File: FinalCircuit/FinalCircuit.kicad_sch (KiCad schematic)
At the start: 54 parts, among them J1 Conn_02x20_Odd_Even, J2 Conn_02x05_Odd_Even, J3 Conn_01x06, U1 LM6172, U10 CD4066BE, U11 CD4066BE, U2 OPA2277, U3 MCP3008, U4 MCP4921, U5 CD4066BE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

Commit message: Almost all connections done. Digital traces seem too long at the moment.
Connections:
- net ADC_CSbar: now also J1.10 (Pin_10); no longer J1.34 (Pin_34)
- net CLK: now also J1.18 (Pin_18); no longer J1.39 (Pin_39)
- net Control1: now also J1.15 (Pin_15); no longer J1.9 (Pin_9)
- net Control10A: now also J1.27 (Pin_27); no longer J1.19 (Pin_19)
- net Control10B: now also J1.21 (Pin_21); no longer J1.15 (Pin_15)
- net Control2: now also J1.39 (Pin_39); no longer J1.6 (Pin_6)
- net Control3: now also J1.37 (Pin_37); no longer J1.8 (Pin_8)
- net Control4: now also J1.17 (Pin_17); no longer J1.10 (Pin_10)
- net Control5: now also J1.7 (Pin_7); no longer J1.14 (Pin_14)
- net Control6: now also J1.8 (Pin_8); no longer J1.16 (Pin_16)
- net Control7: now also J1.9 (Pin_9); no longer J1.5 (Pin_5)
- net Control8: now also J1.6 (Pin_6); no longer J1.7 (Pin_7)
- net Control9A: now also J1.19 (Pin_19); no longer J1.13 (Pin_13)
- net Control9B: now also J1.35 (Pin_35); no longer J1.17 (Pin_17)
- net ControlMain_ReadWrite: now also J1.4 (Pin_4); no longer J1.35 (Pin_35)
- net ControlMain_Reset: now also J1.13 (Pin_13); no longer J1.37 (Pin_37)
- net Control_Hz1A: now also J1.38 (Pin_38); no longer J1.21 (Pin_21)
- net Control_Hz1B: now also J1.34 (Pin_34); no longer J1.23 (Pin_23)
- net Control_Hz2A: now also J1.36 (Pin_36); no longer J1.25 (Pin_25)
- net Control_Hz2B: now also J1.40 (Pin_40); no longer J1.27 (Pin_27)
- net Control_Hz3A: now also J1.23 (Pin_23); no longer J1.31 (Pin_31)
- net Control_Vt1A: now also J1.2 (Pin_2); no longer J1.18 (Pin_18)
- net Control_Vt1B: now also J1.3 (Pin_3); no longer J1.20 (Pin_20)
- net Control_Vt2A: now also J1.5 (Pin_5); no longer J1.22 (Pin_22)
- net Control_Vt2B: now also J1.1 (Pin_1); no longer J1.24 (Pin_24)
- net Control_Vt3A: now also J1.31 (Pin_31); no longer J1.26 (Pin_26)
- net Control_Vt3B: now also J1.25 (Pin_25); no longer J1.28 (Pin_28)
- net DAC_CSbar: now also J1.24 (Pin_24); no longer J1.1 (Pin_1)
- net Din: now also J1.14 (Pin_14); no longer J1.36 (Pin_36)
- net Dout: now also J1.16 (Pin_16); no longer J1.32 (Pin_32)
- net LDACbar: now also J1.32 (Pin_32); no longer J1.3 (Pin_3)
- net SCK: now also J1.26 (Pin_26); no longer J1.2 (Pin_2)
- net SDI: now also J1.28 (Pin_28); no longer J1.4 (Pin_4)

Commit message: Final PCB all routing done, 0 errors. Verification left
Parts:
- removed J2: Conn_02x05_Odd_Even, Connector_PinHeader_2.54mm:PinHeader_2x05_P2.54mm_Vertical, symbol Connector_Generic:Conn_02x05_Odd_Even
- added FB10, FB7, FB8, FB9: FerriteBead, Inductor_SMD:L_0805_2012Metric_Pad1.15x1.40mm_HandSolder, symbol Device:FerriteBead
- added H4: MountingHole, MountingHole:MountingHole_3mm, symbol Mechanical:MountingHole
- added J2: Conn_02x06_Odd_Even, Connector_PinHeader_2.54mm:PinHeader_2x06_P2.54mm_Vertical, symbol Connector_Generic:Conn_02x06_Odd_Even
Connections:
- net +15V: now also FB8.2, J2.1 (Pin_1), J2.2 (Pin_2); no longer C1.1, C2.1, C5.1, C6.1, U1.8 (V+), U2.8 (V+)
- net +5V: now also J2.3 (Pin_3), J2.4 (Pin_4); no longer FB3.2
- net -15V: now also FB9.2, J2.11 (Pin_11), J2.12 (Pin_12); no longer C3.1, C4.1, C7.1, C8.1, U1.4 (V-), U2.4 (V-)
- net -5V: now also J2.10 (Pin_10), J2.9 (Pin_9)
- net GNDD: now also FB10.1, FB7.1
- net PowerGND: now also FB10.2, FB7.2, J2.7 (Pin_7), J2.8 (Pin_8)
- net +5VD renamed +SwitchD
- new net +15VA: C1.1, C2.1, C5.1, C6.1, FB8.1, U1.8 (V+), U2.8 (V+)
- new net +Switch: FB3.2, J2.5 (Pin_5), J2.6 (Pin_6)
- new net -15VA: C3.1, C4.1, C7.1, C8.1, FB9.1, U1.4 (V-), U2.4 (V-)
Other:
- moved on the sheet: FB2

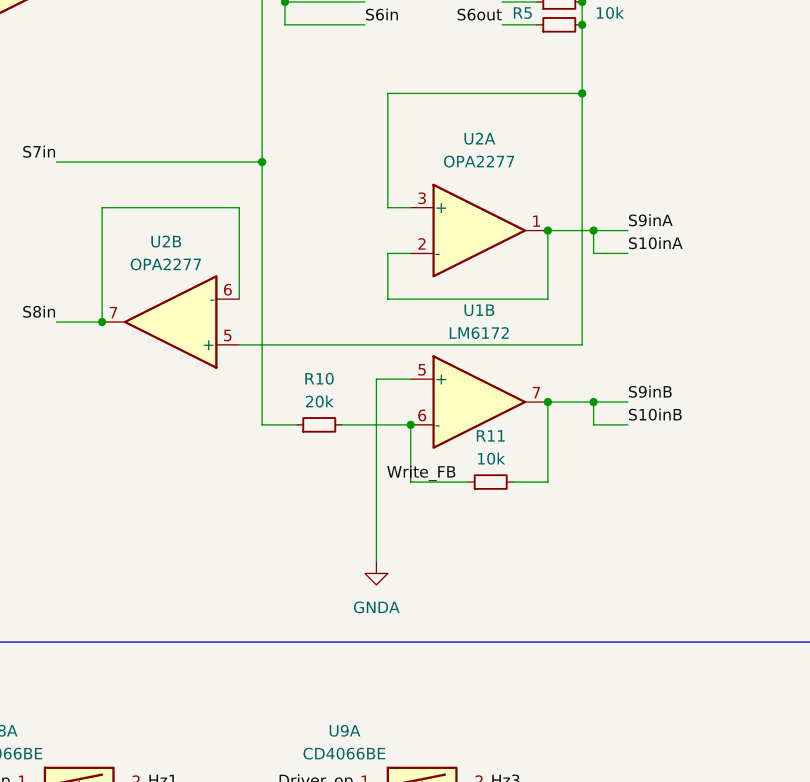
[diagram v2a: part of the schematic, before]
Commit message: Found an error in LM6172 connection. Routing of that is left.
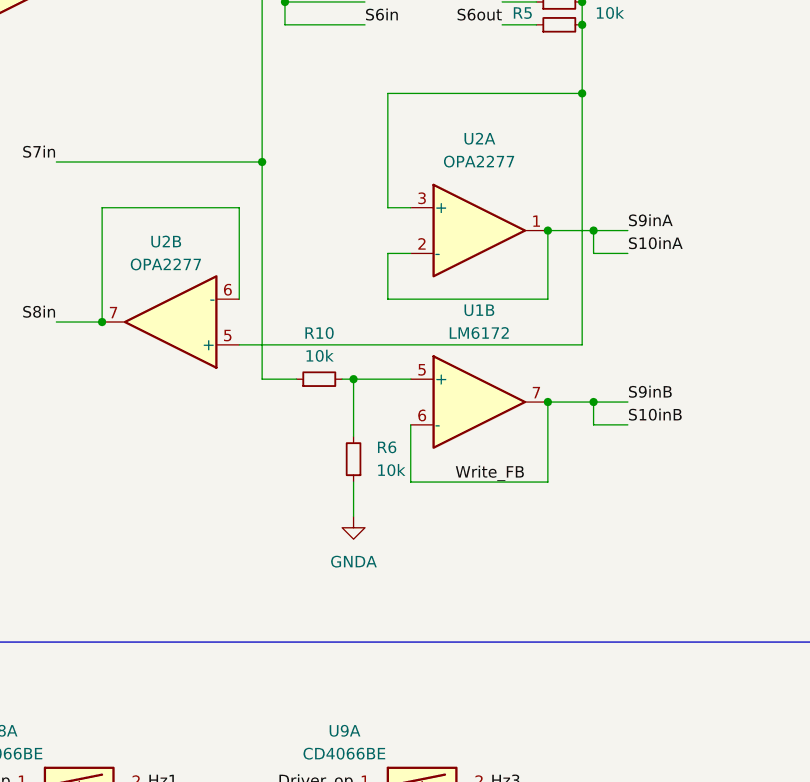
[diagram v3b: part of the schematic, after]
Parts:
- removed R11: 10k, Resistor_SMD:R_1206_3216Metric_Pad1.30x1.75mm_HandSolder, symbol Device:R_Small
- added R6: 10k, Resistor_SMD:R_1206_3216Metric_Pad1.30x1.75mm_HandSolder, symbol Device:R_Small
- R10: value 20k -> 10k
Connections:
- net GNDA: now also R6.1; no longer U1.5 (+)
- net S10inB: now also U1.6 (-)
- net Write_FB: no longer names the net of R10.2
- net Write_FB: now also U1.5 (+), R6.2; no longer U1.6 (-)
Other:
- moved on the sheet: R10
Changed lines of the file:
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@@
 	)
 	(junction
-		(at 135.89 91.44)
-		(diameter 0)
-		(color 0 0 0 0)
-	)
-	(junction
 		(at 151.13 88.9)
 		(diameter 0)
@@
 	)
 	(junction
+		(at 129.54 86.36)
+		(diameter 0)
+		(color 0 0 0 0)
+	)
+	(junction
 		(at 72.39 219.71)
 		(diameter 0)
@@
 	(wire
 		(pts
-			(xy 135.89 97.79) (xy 142.24 97.79)
+			(xy 135.89 97.79) (xy 151.13 97.79)
 		)
 		(stroke
@@
 	(wire
 		(pts
-			(xy 135.89 86.36) (xy 132.08 86.36)
-		)
-		(stroke
-			(width 0)
-			(type default)
-		)
-	)
-	(wire
-		(pts
 			(xy 232.41 144.78) (xy 232.41 148.59)
 		)
@@
 	(wire
 		(pts
-			(xy 128.27 91.44) (xy 135.89 91.44)
-		)
-		(stroke
-			(width 0)
-			(type default)
-		)
-	)
-	(wire
-		(pts
 			(xy 246.38 148.59) (xy 246.38 154.94)
 		)
@@
 	(wire
 		(pts
-			(xy 119.38 91.44) (xy 123.19 91.44)
+			(xy 119.38 86.36) (xy 123.19 86.36)
+		)
+		(stroke
+			(width 0)
+			(type default)
+		)
+	)
+	(wire
+		(pts
+			(xy 129.54 86.36) (xy 135.89 86.36)
 		)
 		(stroke
@@
 	(wire
 		(pts
-			(xy 147.32 97.79) (xy 151.13 97.79)
-		)
-		(stroke
-			(width 0)
-			(type default)
-		)
-	)
-	(wire
-		(pts
-			(xy 132.08 86.36) (xy 132.08 106.68)
+			(xy 128.27 86.36) (xy 129.54 86.36)
 		)
 		(stroke
@@
 	(wire
 		(pts
+			(xy 129.54 97.79) (xy 129.54 101.6)
+		)
+		(stroke
+			(width 0)
+			(type default)
+		)
+	)
+	(wire
+		(pts
 			(xy 62.23 175.26) (xy 62.23 180.34)
 		)
@@
 	(wire
 		(pts
-			(xy 119.38 62.23) (xy 119.38 91.44)
+			(xy 119.38 62.23) (xy 119.38 86.36)
 		)
 		(stroke
@@
 	(wire
 		(pts
+			(xy 129.54 86.36) (xy 129.54 92.71)
+		)
+		(stroke
+			(width 0)
+			(type default)
+		)
+	)
+	(wire
+		(pts
 			(xy 52.07 67.31) (xy 55.88 67.31)
 		)
@@
 	)
 	(label "Write_FB"
-		(at 140.97 97.79 180)
+		(at 148.59 97.79 180)
 		(fields_autoplaced yes)
 		(effects
@@
 	)
 	(symbol
-		(lib_id "Device:R_Small")
-		(at 144.78 97.79 90)
-		(unit 1)
-		(exclude_from_sim no)
-		(in_bom yes)
-		(on_board yes)
-		(dnp no)
-		(fields_autoplaced yes)
-		(property "Reference" "R11"
-			(at 144.78 92.71 90)
-			(effects
-				(font
-					(size 1.27 1.27)
-				)
-			)
-		)
-		(property "Value" "10k"
-			(at 144.78 95.25 90)
-			(effects
-				(font
-					(size 1.27 1.27)
-				)
-			)
-		)
-		(property "Footprint" "Resistor_SMD:R_1206_3216Metric_Pad1.30x1.75mm_HandSolder"
-			(at 144.78 97.79 0)
-			(effects
-				(font
-					(size 1.27 1.27)
-				)
-				(hide yes)
-			)
-		)
-		(property "Datasheet" "~"
-			(at 144.78 97.79 0)
-			(effects
-				(font
-					(size 1.27 1.27)
-				)
-				(hide yes)
-			)
-		)
-		(property "Description" "Resistor, small symbol"
-			(at 144.78 97.79 0)
-			(effects
-				(font
-					(size 1.27 1.27)
-				)
-				(hide yes)
-			)
-		)
-		(pin "2"
-		)
-		(pin "1"
-		)
-		(instances
-			(project "FinalCircuit"
-				(path "/ed26f7ee-1e82-4f03-9269-cad330ded895"
-					(reference "R11")
-					(unit 1)
-				)
-			)
-		)
-	)
-	(symbol
 		(lib_id "power:PWR_FLAG")
 		(at 350.52 66.04 180)
@@
 	)
 	(symbol
+		(lib_id "Device:R_Small")
+		(at 129.54 95.25 180)
+		(unit 1)
+		(exclude_from_sim no)
+		(in_bom yes)
+		(on_board yes)
+		(dnp no)
+		(fields_autoplaced yes)
+		(property "Reference" "R6"
+			(at 132.08 93.9799 0)
+			(effects
+				(font
+					(size 1.27 1.27)
+				)
+				(justify right)
+			)
+		)
+		(property "Value" "10k"
+			(at 132.08 96.5199 0)
+			(effects
+				(font
+					(size 1.27 1.27)
+				)
+				(justify right)
+			)
+		)
+		(property "Footprint" "Resistor_SMD:R_1206_3216Metric_Pad1.30x1.75mm_HandSolder"
+			(at 129.54 95.25 0)
+			(effects
+				(font
+					(size 1.27 1.27)
+				)
+				(hide yes)
+			)
+		)
+		(property "Datasheet" "~"
+			(at 129.54 95.25 0)
+			(effects
+				(font
+					(size 1.27 1.27)
+				)
+				(hide yes)
+			)
+		)
+		(property "Description" "Resistor, small symbol"
+			(at 129.54 95.25 0)
+			(effects
+				(font
+					(size 1.27 1.27)
+				)
+				(hide yes)
+			)
+		)
+		(pin "2"
+		)
+		(pin "1"
+		)
+		(instances
+			(project "FinalCircuit"
+				(path "/ed26f7ee-1e82-4f03-9269-cad330ded895"
+					(reference "R6")
+					(unit 1)
+				)
+			)
+		)
+	)
+	(symbol
 		(lib_id "power:GNDD")
 		(at 123.19 271.78 0)
@@
 	(symbol
 		(lib_id "power:GNDA")
-		(at 132.08 106.68 0)
+		(at 129.54 101.6 0)
 		(unit 1)
 		(exclude_from_sim no)
@@
 		(fields_autoplaced yes)
 		(property "Reference" "#PWR08"
-			(at 132.08 113.03 0)
+			(at 129.54 107.95 0)
 			(effects
 				(font
@@
 		)
 		(property "Value" "GNDA"
-			(at 132.08 111.76 0)
+			(at 129.54 106.68 0)
 			(effects
 				(font
@@
 		)
 		(property "Footprint" ""
-			(at 132.08 106.68 0)
+			(at 129.54 101.6 0)
 			(effects
 				(font
@@
 		)
 		(property "Datasheet" ""
-			(at 132.08 106.68 0)
+			(at 129.54 101.6 0)
 			(effects
 				(font
@@
 		)
 		(property "Description" "Power symbol creates a global label with name \"GNDA\" , analog ground"
-			(at 132.08 106.68 0)
+			(at 129.54 101.6 0)
 			(effects
 				(font
@@
 	(symbol
 		(lib_id "Device:R_Small")
-		(at 125.73 91.44 90)
+		(at 125.73 86.36 90)
 		(unit 1)
 		(exclude_from_sim no)
@@
 		(fields_autoplaced yes)
 		(property "Reference" "R10"
-			(at 125.73 86.36 90)
+			(at 125.73 81.28 90)
 			(effects
 				(font
@@
 			)
 		)
-		(property "Value" "20k"
-			(at 125.73 88.9 90)
+		(property "Value" "10k"
+			(at 125.73 83.82 90)
 			(effects
 				(font
@@
 		)
 		(property "Footprint" "Resistor_SMD:R_1206_3216Metric_Pad1.30x1.75mm_HandSolder"
-			(at 125.73 91.44 0)
+			(at 125.73 86.36 0)
 			(effects
 				(font
@@
 		)
 		(property "Datasheet" "~"
-			(at 125.73 91.44 0)
+			(at 125.73 86.36 0)
 			(effects
 				(font
@@
 		)
 		(property "Description" "Resistor, small symbol"
-			(at 125.73 91.44 0)
+			(at 125.73 86.36 0)
 			(effects
 				(font
